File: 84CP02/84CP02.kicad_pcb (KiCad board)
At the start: 4 copper layers, 25.7 x 76.7 mm, 7 parts, among them J1 Conn_01x30, J2 Conn_01x30, J3 Conn_02x05_Odd_Even, J4 Conn_02x03_Odd_Even, U1 XC9572XL-VQ64

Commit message: First attempts at routing the CP02 baseboard
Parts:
- moved C2 36.2 mm to (141.5, 58.0)
- moved C1 36.2 mm to (152.7, 58.0)
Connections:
- U1 pad 1: unconnected-(U1-P1-Pad1) -> /J2-17
- U1 pad 10: unconnected-(U1-P10-Pad10) -> /J2-16
- U1 pad 11: unconnected-(U1-P11-Pad11) -> /J2-23
- U1 pad 12: unconnected-(U1-P12-Pad12) -> /J2-28
- U1 pad 13: unconnected-(U1-P13-Pad13) -> /J2-13
- U1 pad 15: unconnected-(U1-I/O/GCK1-Pad15) -> /J2-22
- U1 pad 16: unconnected-(U1-I/O/GCK2-Pad16) -> /J1-23
- U1 pad 17: unconnected-(U1-I/O/GCK3-Pad17) -> /J2-19
- U1 pad 18: unconnected-(U1-P18-Pad18) -> /J2-25
- U1 pad 19: unconnected-(U1-P19-Pad19) -> /J2-27
- U1 pad 2: unconnected-(U1-I/O/GTS2-Pad2) -> /J1-13
- U1 pad 20: unconnected-(U1-P20-Pad20) -> /J2-26
- U1 pad 22: unconnected-(U1-P22-Pad22) -> /J2-5
- U1 pad 23: unconnected-(U1-P23-Pad23) -> /J2-14
- U1 pad 24: unconnected-(U1-P24-Pad24) -> /J2-6
- U1 pad 25: unconnected-(U1-P25-Pad25) -> /J1-9
- U1 pad 27: unconnected-(U1-P27-Pad27) -> /J2-12
- U1 pad 31: unconnected-(U1-P31-Pad31) -> /J1-15
- U1 pad 32: unconnected-(U1-P32-Pad32) -> /J1-25
- U1 pad 33: unconnected-(U1-P33-Pad33) -> /J1-22
- U1 pad 34: unconnected-(U1-P34-Pad34) -> /J1-17
- U1 pad 35: unconnected-(U1-P35-Pad35) -> /J1-10
- U1 pad 36: VCC -> /J1-3
- U1 pad 38: unconnected-(U1-P38-Pad38) -> /J2-20
- U1 pad 39: unconnected-(U1-P39-Pad39) -> /J1-8
- U1 pad 4: unconnected-(U1-P4-Pad4) -> /J2-8
- U1 pad 40: unconnected-(U1-P40-Pad40) -> /J2-15
- U1 pad 42: unconnected-(U1-P42-Pad42) -> /J2-11
- U1 pad 43: unconnected-(U1-P43-Pad43) -> /J2-4
- U1 pad 44: unconnected-(U1-P44-Pad44) -> /J1-26
- U1 pad 45: unconnected-(U1-P45-Pad45) -> /J1-12
- U1 pad 46: unconnected-(U1-P46-Pad46) -> /J1-21
- U1 pad 47: unconnected-(U1-P47-Pad47) -> /J1-24
- U1 pad 48: unconnected-(U1-P48-Pad48) -> /J1-5
- U1 pad 49: unconnected-(U1-P49-Pad49) -> /J2-7
- U1 pad 5: unconnected-(U1-I/O/GTS1-Pad5) -> /J1-14
- U1 pad 50: unconnected-(U1-P50-Pad50) -> /J2-10
- U1 pad 51: unconnected-(U1-P51-Pad51) -> /J2-9
- U1 pad 52: unconnected-(U1-P52-Pad52) -> /J1-7
- U1 pad 56: unconnected-(U1-P56-Pad56) -> /J1-16
- U1 pad 57: unconnected-(U1-P57-Pad57) -> /J1-28
- U1 pad 58: unconnected-(U1-P58-Pad58) -> /J1-18
- U1 pad 59: unconnected-(U1-P59-Pad59) -> /J1-20
- U1 pad 6: unconnected-(U1-P6-Pad6) -> /J1-6
- U1 pad 60: unconnected-(U1-P60-Pad60) -> /J2-24
- U1 pad 61: VCC -> /J1-4
- U1 pad 62: unconnected-(U1-P62-Pad62) -> /J2-3
- U1 pad 63: unconnected-(U1-P63-Pad63) -> /J2-21
- U1 pad 64: unconnected-(U1-I/O/GSR-Pad64) -> /J1-19
- U1 pad 7: unconnected-(U1-P7-Pad7) -> /J2-18
- U1 pad 8: unconnected-(U1-P8-Pad8) -> /J1-11
- U1 pad 9: unconnected-(U1-P9-Pad9) -> /J1-27
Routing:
- net /J1-3: track 0.00 -> 49.6 mm, vias 0 -> 2
- net /J1-4: track 0.00 -> 39.1 mm, vias 0 -> 2
- net /J2-3: track 0.00 -> 34.9 mm, vias 0 -> 2
- net /J1-10: track 0.00 -> 32.3 mm, vias 0 -> 2
- net /J2-21: track 0.00 -> 30.8 mm, vias 0 -> 2
- net VCC: track 0.00 -> 28.9 mm
- net /J1-19: track 0.00 -> 27.9 mm, vias 0 -> 2
- net /J2-17: track 0.00 -> 27.9 mm, vias 0 -> 2
- net /J1-25: track 0.00 -> 27.8 mm, vias 0 -> 2
- net /J1-22: track 0.00 -> 24.1 mm, vias 0 -> 2
- net /J1-17: track 0.00 -> 20.1 mm, vias 0 -> 3
- net /J1-15: track 0.00 -> 17.6 mm, vias 0 -> 1
- net GND: track 0.00 -> 13.3 mm

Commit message: Ongoing routing
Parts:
- C1, C2: moved to F.Cu
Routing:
- net /J2-24: track 0.00 -> 64.2 mm, vias 0 -> 3
- net GND: track 13.3 -> 72.1 mm
- net /J2-13: track 0.00 -> 55.4 mm, vias 0 -> 3
- net /J1-28: track 0.00 -> 52.9 mm, vias 0 -> 3
- net /J2-27: track 0.00 -> 50.0 mm, vias 0 -> 3
- net /J1-21: track 0.00 -> 49.7 mm, vias 0 -> 4
- net /J2-28: track 0.00 -> 48.7 mm, vias 0 -> 3
- net /J1-5: track 0.00 -> 45.9 mm, vias 0 -> 3
- net VCC: track 28.9 -> 73.7 mm
- net /J1-20: track 0.00 -> 44.6 mm, vias 0 -> 3
- net Net-(J3-Pin_7): track 0.00 -> 43.8 mm, vias 0 -> 2
- net /J1-26: track 0.00 -> 41.5 mm, vias 0 -> 1
- net /J2-26: track 0.00 -> 41.0 mm, vias 0 -> 1
- net /J2-25: track 0.00 -> 41.0 mm, vias 0 -> 1
- net /J1-18: track 0.00 -> 40.8 mm, vias 0 -> 3
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
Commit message: Tagging this commit as failed_routing_1 before backing out and trying a different approach.
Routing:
- net /J2-14: track 0.00 -> 92.6 mm, vias 0 -> 5
- net /J1-8: track 0.00 -> 50.8 mm, vias 0 -> 3
- net /J2-5: track 0.00 -> 50.3 mm, vias 0 -> 3
- net /J2-16: track 0.00 -> 44.3 mm, vias 0 -> 1
- net /J1-7: track 0.00 -> 40.3 mm, vias 0 -> 1
- net /J2-17: track 0.00 -> 37.1 mm, vias 0 -> 1
- net /J2-8: track 0.00 -> 35.6 mm, vias 0 -> 1
- net /J1-15: track 0.00 -> 32.7 mm, vias 0 -> 1
- net /J2-18: track 0.00 -> 27.0 mm, vias 0 -> 1
- net VCC: track 73.7 -> 99.4 mm, vias 0 -> 2
- net GND: track 72.1 -> 96.1 mm, vias 0 -> 4
- net /J2-9: track 0.00 -> 22.5 mm, vias 0 -> 1
- net /J2-7: track 0.00 -> 22.2 mm
- net /J2-10: track 0.00 -> 19.0 mm, vias 0 -> 1
- net /J1-14: track 0.00 -> 17.6 mm, vias 0 -> 1
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
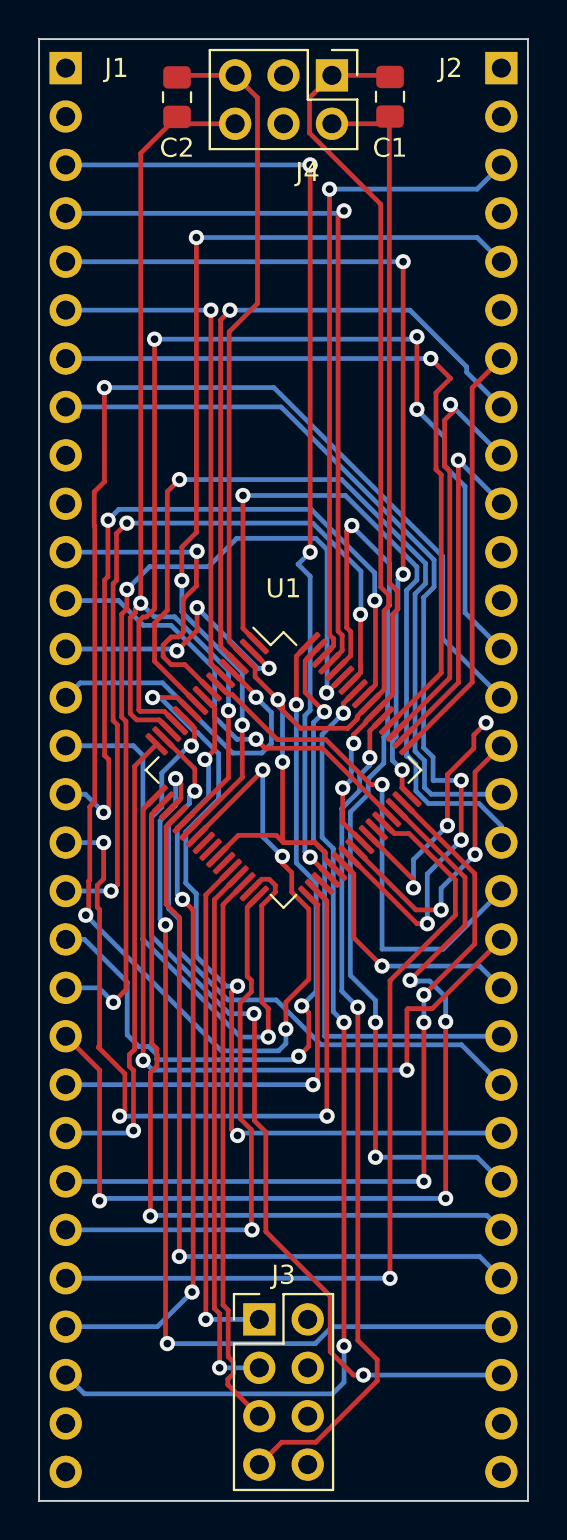
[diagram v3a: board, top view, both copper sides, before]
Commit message: 84CP02 board is routed and all DRC errors and warnings are fixed.
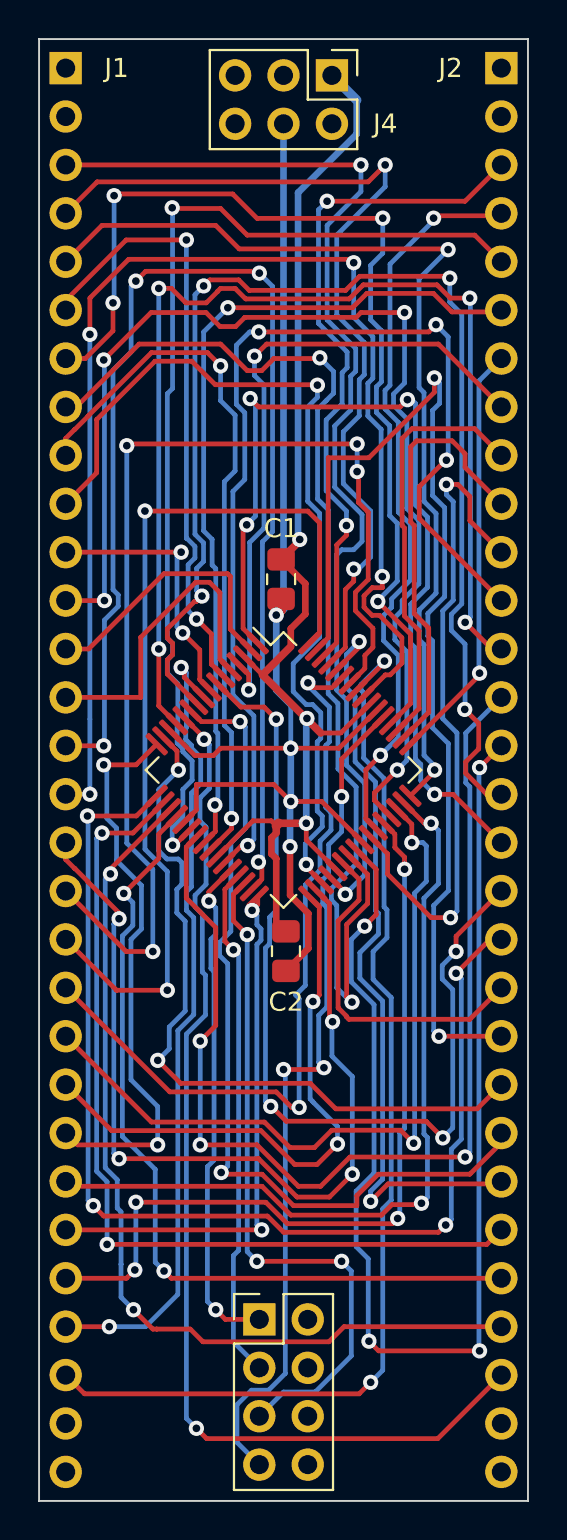
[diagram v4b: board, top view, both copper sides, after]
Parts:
- moved C2 45.2 mm to (147.2, 102.8)
- moved C1 26.0 mm to (146.9, 83.3)
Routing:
- net /J2-12: track 0.00 -> 57.0 mm, vias 0 -> 4
- net /J2-15: track 15.7 -> 66.2 mm, vias 2 -> 4
- net /J1-10: track 0.00 -> 47.4 mm, vias 0 -> 2
- net /J2-6: track 0.00 -> 44.3 mm, vias 0 -> 2
- net /J2-4: track 0.00 -> 39.2 mm, vias 0 -> 2
- net /J1-12: track 23.2 -> 61.1 mm, vias 1 -> 4
- net /J1-9: track 0.00 -> 37.7 mm, vias 0 -> 2
- net VCC: track 99.4 -> 64.2 mm, vias 2 -> 3
- net /J1-15: track 32.7 -> 67.3 mm, vias 1 -> 4
- net /J2-14: track 92.6 -> 57.9 mm, vias 5 -> 3
- net /J1-16: track 40.4 -> 68.4 mm, vias 3 -> 4
- net /J2-21: track 30.7 -> 57.7 mm, vias 1 -> 2
- net GND: track 96.1 -> 71.5 mm
- net /J2-16: track 44.3 -> 67.6 mm, vias 1 -> 4
- net /J2-19: track 37.9 -> 60.6 mm, vias 2 -> 4
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
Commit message: A few polishing changes and rerun the Design Rule Checker
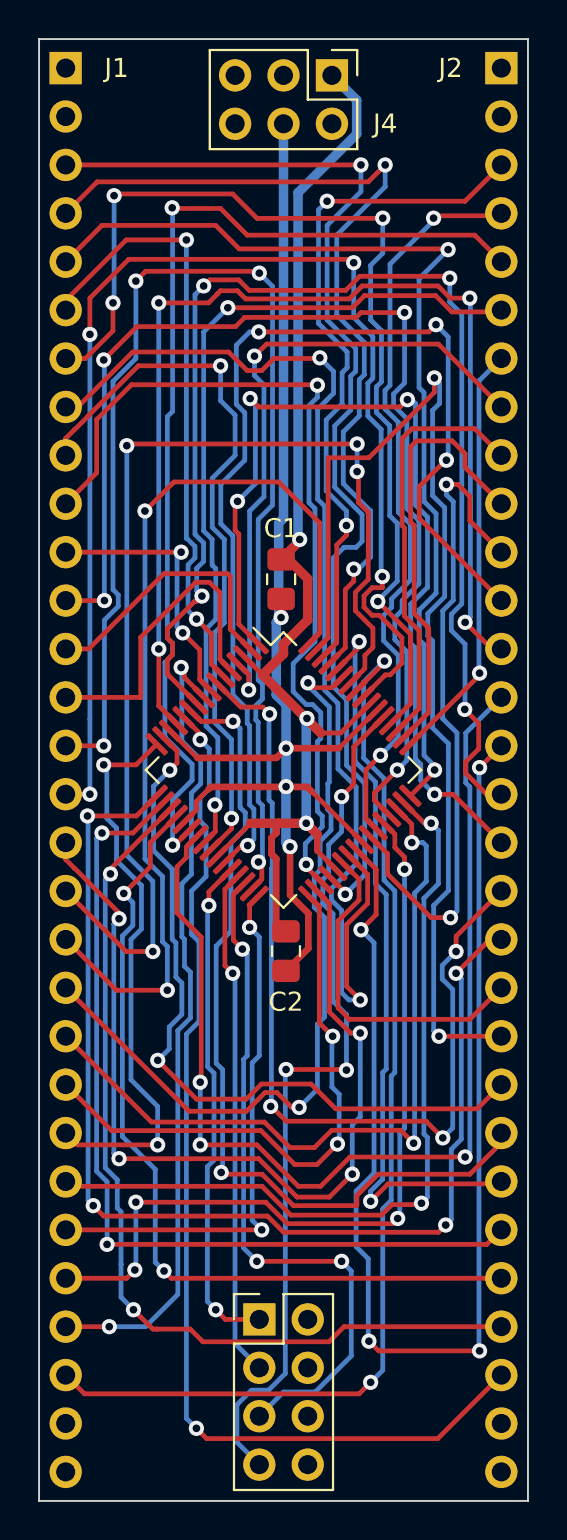
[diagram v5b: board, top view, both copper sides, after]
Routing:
- net /J1-10: track 47.4 -> 46.1 mm
- net Net-(J3-Pin_7): track 45.1 -> 46.3 mm
- net /J1-19: track 48.0 -> 49.3 mm
- net /J2-13: track 60.7 -> 59.4 mm
- net /J1-20: track 40.0 -> 41.0 mm
- net /J2-24: track 40.8 -> 39.8 mm
- net /J1-17: track 47.3 -> 47.9 mm
- net /J1-12: track 61.1 -> 60.5 mm
- net /J1-28: track 58.9 -> 58.3 mm
- net /J2-12: track 57.0 -> 57.5 mm

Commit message: commit Gerbers for this project
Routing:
- net GND: track 71.0 -> 75.0 mm
- net Net-(J3-Pin_7): track 46.3 -> 47.0 mm
- net /J2-18: track 48.5 -> 49.1 mm
- added copper zone on F.Cu, net GND
